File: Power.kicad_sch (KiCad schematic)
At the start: 17 parts, among them J2 Barrel_Jack_Switch_Pin3Ring, U3 AP2127N-3.3, U6 MC78LC50NTR

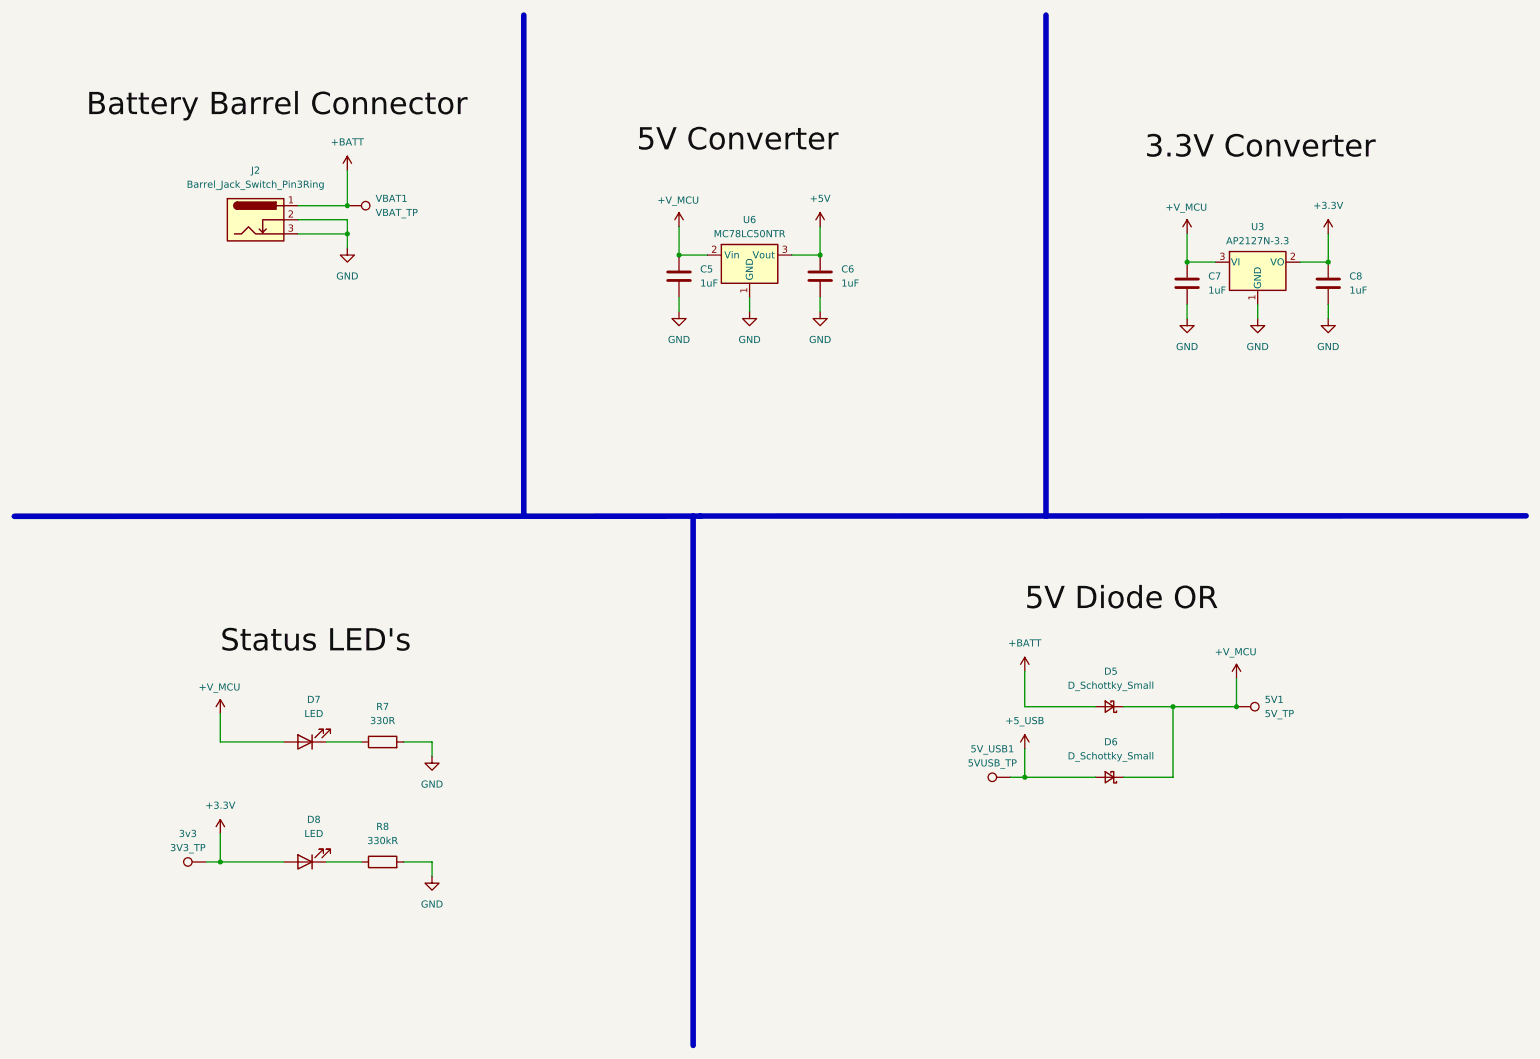
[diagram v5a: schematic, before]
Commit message: Updated to use boost converters
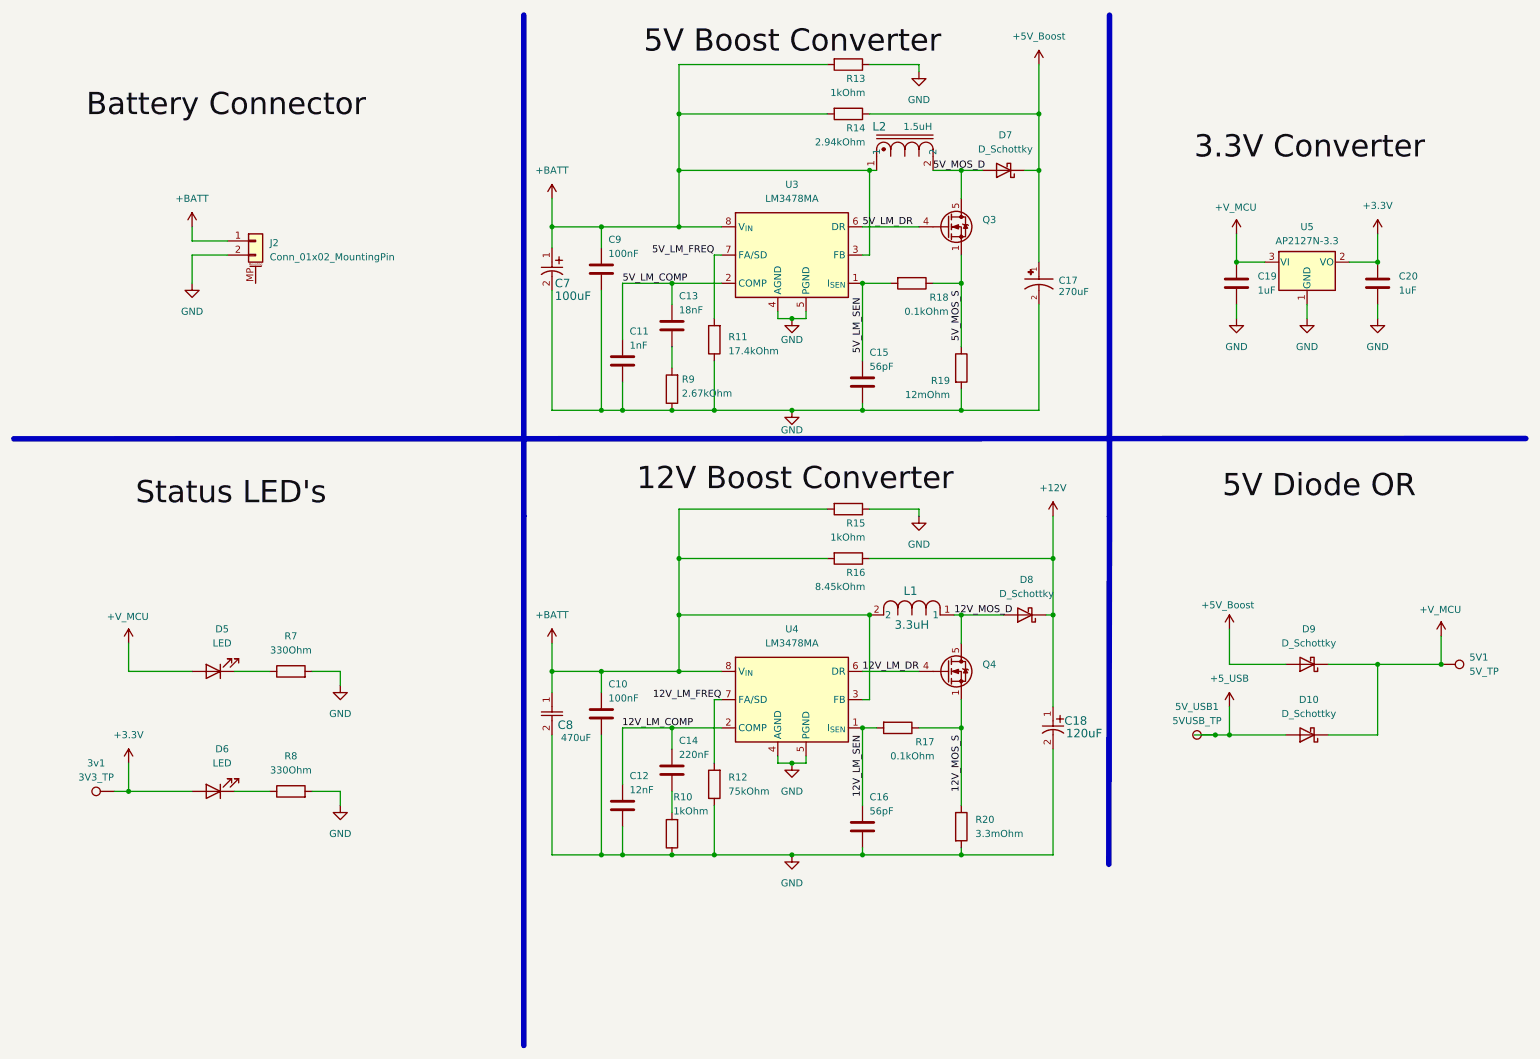
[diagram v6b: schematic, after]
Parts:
- removed C5, C6: 1uF, Capacitor_SMD:C_0603_1608Metric_Pad1.08x0.95mm_HandSolder, symbol Device:C
- removed D5, D6: D_Schottky_Small, Diode_SMD:D_SOD-523, symbol Device:D_Schottky_Small
- removed J2: Barrel_Jack_Switch_Pin3Ring, Connector_BarrelJack:BarrelJack_Kycon_KLDX-0202-xC_Horizontal, symbol Connector:Barrel_Jack_Switch_Pin3Ring
- removed U6: MC78LC50NTR, Package_TO_SOT_SMD:SOT-23-5, symbol Regulator_Linear:MC78LC50NTR
- removed VBAT1: VBAT_TP, TestPoint:TestPoint_Pad_D2.0mm, symbol Connector:TestPoint
- added C10, C9: 100nF, Capacitor_SMD:C_0603_1608Metric_Pad1.08x0.95mm_HandSolder, symbol Device:C
- added C11: 1nF, Capacitor_SMD:C_0603_1608Metric_Pad1.08x0.95mm_HandSolder, symbol Device:C
- added C12: 12nF, Capacitor_SMD:C_0603_1608Metric_Pad1.08x0.95mm_HandSolder, symbol Device:C
- added C13: 18nF, Capacitor_SMD:C_0603_1608Metric_Pad1.08x0.95mm_HandSolder, symbol Device:C
- added C14: 220nF, Capacitor_SMD:C_0603_1608Metric_Pad1.08x0.95mm_HandSolder, symbol Device:C
- added C15, C16: 56pF, Capacitor_SMD:C_0603_1608Metric_Pad1.08x0.95mm_HandSolder, symbol Device:C
- added C17: 16SVPG270M, Insight:CAP_16SVPG270M, symbol Insight:16SVPG270M
- added C18: 20SVPF120M, Insight:PCAP_SVP_C6_PAN, symbol Insight:20SVPF120M
- added C7: T520A107M006ATE025, Insight:CAPMP3.4X1.6_1.8N_KEM, symbol Insight:T520A107M006ATE025
- added C8: UUD1E471MNL1GS, U2-R_NCH, symbol Insight:UUD1E471MNL1GS
- added D10, D7, D8, D9: D_Schottky, Diode_SMD:D_SMC, symbol Device:D_Schottky
- added J2: Conn_01x02_MountingPin, Connector_Hirose:Hirose_DF3EA-02P-2H_1x02-1MP_P2.00mm_Horizontal, symbol Connector_Generic_MountingPin:Conn_01x02_MountingPin
- added L1: IHLP6767GZER3R3M51, IND_IHLP-6767GZ_VIS, symbol Insight:IHLP6767GZER3R3M51
- added L2: DR1040-1R5-R, Insight:DR1040, symbol Insight:DR1040-1R5-R
- added Q3, Q4: CSD16321Q5, Package_TO_SOT_SMD:TDSON-8-1, symbol Transistor_FET:CSD16321Q5
- added R10, R13, R15: 1kOhm, Resistor_SMD:R_0603_1608Metric_Pad0.98x0.95mm_HandSolder, symbol Device:R
- added R11: 17.4kOhm, Resistor_SMD:R_0603_1608Metric_Pad0.98x0.95mm_HandSolder, symbol Device:R
- added R12: 75kOhm, Resistor_SMD:R_0603_1608Metric_Pad0.98x0.95mm_HandSolder, symbol Device:R
- added R14: 2.94kOhm, Resistor_SMD:R_0603_1608Metric_Pad0.98x0.95mm_HandSolder, symbol Device:R
- added R16: 8.45kOhm, Resistor_SMD:R_0603_1608Metric_Pad0.98x0.95mm_HandSolder, symbol Device:R
- added R17, R18: 0.1kOhm, Resistor_SMD:R_0603_1608Metric_Pad0.98x0.95mm_HandSolder, symbol Device:R
- added R19: 12mOhm, Resistor_SMD:R_0603_1608Metric_Pad0.98x0.95mm_HandSolder, symbol Device:R
- added R20: 3.3mOhm, Resistor_SMD:R_2512_6332Metric_Pad1.40x3.35mm_HandSolder, symbol Device:R
- added R9: 2.67kOhm, Resistor_SMD:R_0603_1608Metric_Pad0.98x0.95mm_HandSolder, symbol Device:R
- added U3, U4: LM3478MA, Package_SO:SOIC-8_3.9x4.9mm_P1.27mm, symbol Regulator_Controller:LM3478MA
- R7: value 330R -> 330Ohm
- R8: value 330kR -> 330Ohm
- renumbered 3v3 to 3v1, C7 to C19, C8 to C20, D7 to D5, D8 to D6, U3 to U5
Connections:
- net +5_USB: now also D10.2 (A)
- net +BATT: now also C10.1, C7.1, C8.1, C9.1, J2.1 (Pin_1), L1.2, L2.1, R13.2, R14.2, R15.2, R16.2, U3.3 (FB), U3.8 (V_{IN}), U4.3 (FB), U4.8 (V_{IN})
- net +V_MCU: now also D10.1 (K), D9.1 (K)
- net GND: now also C10.2, C11.2, C12.2, C15.2, C16.2, C17.2, C18.2, C7.2, C8.2, C9.2, J2.2 (Pin_2), R10.1, R11.1, R12.1, R13.1, R15.1, R19.2, R20.2, R9.1, U3.4 (AGND), U3.5 (PGND), U4.4 (AGND), U4.5 (PGND)
- new net: C14.2, R10.2
- new net: C13.2, R9.2
- new net +12V: C18.1, D8.1 (K), R16.1
- new net +5V_Boost: C17.1, D7.1 (K), D9.2 (A), R14.1
- new net 12V_LM_COMP: C12.1, C14.1, U4.2 (COMP)
- new net 12V_LM_DR: Q4.4 (G), U4.6 (DR)
- new net 12V_LM_FREQ: R12.2, U4.7 (FA/SD)
- new net 12V_LM_SEN: C16.1, R17.2, U4.1 (I_{SEN})
- new net 12V_MOS_D: D8.2 (A), L1.1, Q4.5 (D)
- new net 12V_MOS_S: Q4.1 (S), Q4.2 (S), Q4.3 (S), R17.1, R20.1
- new net 5V_LM_COMP: C11.1, C13.1, U3.2 (COMP)
- new net 5V_LM_DR: Q3.4 (G), U3.6 (DR)
- new net 5V_LM_FREQ: R11.2, U3.7 (FA/SD)
- new net 5V_LM_SEN: C15.1, R18.2, U3.1 (I_{SEN})
- new net 5V_MOS_D: D7.2 (A), L2.2, Q3.5 (D)
- new net 5V_MOS_S: Q3.1 (S), Q3.2 (S), Q3.3 (S), R18.1, R19.1
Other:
- moved on the sheet: 3v1, 5V1, 5V_USB1, C19, C20, D5, D6, R7, R8, U5
